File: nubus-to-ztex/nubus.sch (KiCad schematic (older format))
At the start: 54 parts, among them J4 0850030567 (DIN 41612C 3x32 p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, U1 74LVT125PW,118, U13 SN74CB3T3245PWR, U14 SN74CB3T3245PWR, U15 SN74CB3T3245PWR, U2 74LVT125PW,118, U3 74LVT125PW,118, U5 74LVT245BPW,118, U6 74LVT245BPW,118, U7 74LVT245BPW,118, U8 74LVT245BPW,118

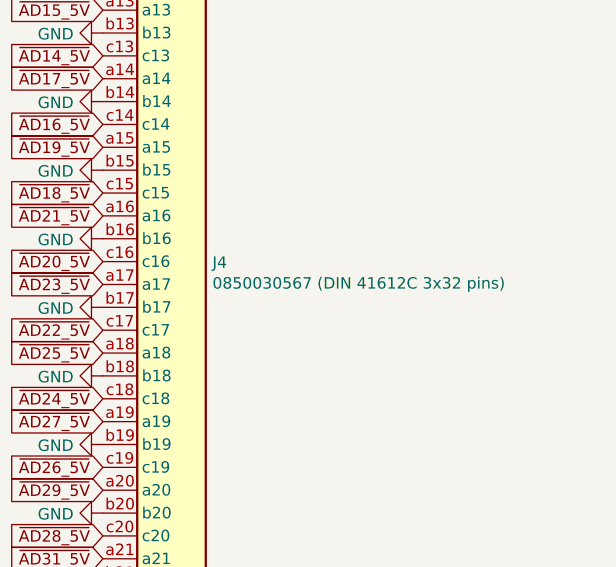
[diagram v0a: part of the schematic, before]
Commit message: more THT->SMT, lexx expensive parts/assembly (?)
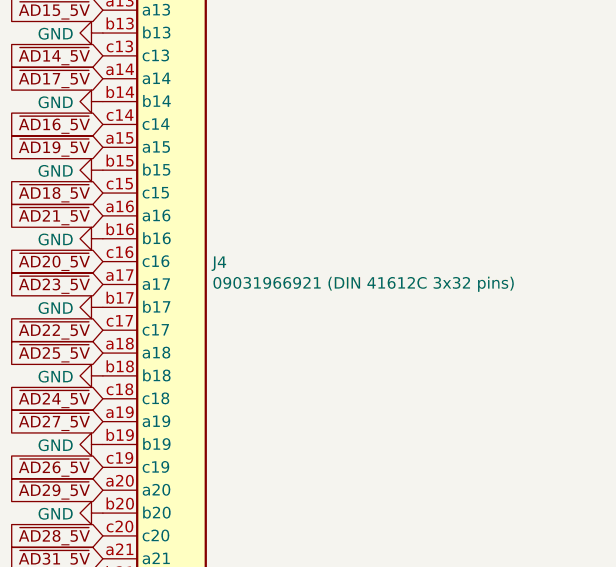
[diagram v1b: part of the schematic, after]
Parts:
- J4: value 0850030567 (DIN 41612C 3x32 pins) -> 09031966921 (DIN 41612C 3x32 pins); MPN 0850030567 -> 09033966921; MPN (Molex) (none) -> 85003-0567; MPN alias 85003-0567 -> (none); Notes (Harting) (none) -> Loads of variants...; URL https://www.mouser.fr/ProductDetail/Molex/85003-0567?qs=U4p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 -> https://www.mouser.fr/ProductDetail/HARTING/09031966921?qs=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
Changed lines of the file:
@@
 P 22250 5750
 F 0 "J4" H 22429 5846 50  0000 L CNN
-F 1 "0850030567 (DIN 41612C 3x32 pins)" H 22429 5755 50  0000 L CNN
+F 1 "09031966921 (DIN 41612C 3x32 pins)" H 22429 5755 50  0000 L CNN
 F 2 "For_SeeedStudio:DIN41612_C_3x32_Male_Horizontal_THT" H 22250 5800 50  0001 C CNN
 F 3 " ~" H 22250 5800 50  0001 C CNN
-F 4 "85003-0567" H 22250 5750 50  0001 C CNN "MPN alias"
-F 5 "https://www.mouser.fr/ProductDetail/Molex/85003-0567?qs=U4pz39agNJB6P1oBpJ4bJA%3D%3D" H 22250 5750 50  0001 C CNN "URL"
+F 4 "85003-0567" H 22250 5750 50  0001 C CNN "MPN (Molex)"
+F 5 "https://www.mouser.fr/ProductDetail/HARTING/09031966921?qs=gIpPgrDBK%2Fho4yEpoERymA%3D%3D" H 22250 5750 50  0001 C CNN "URL"
 F 6 "DIN-096CPC-RR1-HM" H 22250 5750 50  0001 C CNN "MPN (3M)"
 F 7 "RR1L would also work (for .062 PCBs)" H 22250 5750 50  0001 C CNN "Notes (3M)"
 F 8 "09033967921" H 22250 5750 50  0001 C CNN "MPN (Harting)"
 F 9 "09033966921" H 22250 5750 50  0001 C CNN "MPN (Harting 2)"
-F 10 "0850030567" H 22250 5750 50  0001 C CNN "MPN"
+F 10 "09033966921" H 22250 5750 50  0001 C CNN "MPN"
+F 11 "Loads of variants..." H 22250 5750 50  0001 C CNN "Notes (Harting)"
 	1    22250 5750
 	1    0    0    -1

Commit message: minor cleanups
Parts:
- C12, C14, C17, C18, C19, C30, C4, C5, C6, C8: LCSC ? -> (none)
- D10, D6, D7, D8, D9: value YELLOW Led -> YELLOW Led 0805
- D11, D12, D13, D14: value GREEN Led -> GREEN Led 0805
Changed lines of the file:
@@
 F 6 "603-CC603KRX7R8BB104" H 17550 2500 50  0001 C CNN "Mouser"
 F 7 "?" H 17550 2500 50  0001 C CNN "Digikey"
-F 8 "?" H 17550 2500 50  0001 C CNN "LCSC"
+F 8 "" H 17550 2500 50  0001 C CNN "LCSC"
 F 9 "?" H 17550 2500 50  0001 C CNN "Koncar"
 F 10 "TB" H 17550 2500 50  0001 C CNN "Side"
@@
 F 6 "603-CC603KRX7R8BB104" H 15550 2500 50  0001 C CNN "Mouser"
 F 7 "?" H 15550 2500 50  0001 C CNN "Digikey"
-F 8 "?" H 15550 2500 50  0001 C CNN "LCSC"
+F 8 "" H 15550 2500 50  0001 C CNN "LCSC"
 F 9 "?" H 15550 2500 50  0001 C CNN "Koncar"
 F 10 "TB" H 15550 2500 50  0001 C CNN "Side"
@@
 F 6 "603-CC603KRX7R8BB104" H 13500 2500 50  0001 C CNN "Mouser"
 F 7 "?" H 13500 2500 50  0001 C CNN "Digikey"
-F 8 "?" H 13500 2500 50  0001 C CNN "LCSC"
+F 8 "" H 13500 2500 50  0001 C CNN "LCSC"
 F 9 "?" H 13500 2500 50  0001 C CNN "Koncar"
 F 10 "TB" H 13500 2500 50  0001 C CNN "Side"
@@
 F 6 "603-CC603KRX7R8BB104" H 11450 2500 50  0001 C CNN "Mouser"
 F 7 "?" H 11450 2500 50  0001 C CNN "Digikey"
-F 8 "?" H 11450 2500 50  0001 C CNN "LCSC"
+F 8 "" H 11450 2500 50  0001 C CNN "LCSC"
 F 9 "?" H 11450 2500 50  0001 C CNN "Koncar"
 F 10 "TB" H 11450 2500 50  0001 C CNN "Side"
@@
 AR Path="/618F532C/61D85DFA" Ref="D11"  Part="1"
 F 0 "D11" H 16050 7950 50  0000 C CNN
-F 1 "GREEN Led" H 16100 7700 50  0000 R CNN
+F 1 "GREEN Led 0805" H 16100 7700 50  0000 R CNN
 F 2 "LED_SMD:LED_0805_2012Metric" H 16050 7850 50  0001 C CNN
 F 3 "https://www.lcsc.com/product-detail/Light-Emitting-Diodes-LED_Lite-On-LTST-C170KGKT_C98221.html" H 16050 7850 50  0001 C CNN
@@
 AR Path="/618F532C/61D85E17" Ref="D12"  Part="1"
 F 0 "D12" H 16050 8450 50  0000 C CNN
-F 1 "GREEN Led" H 16100 8200 50  0000 R CNN
+F 1 "GREEN Led 0805" H 16100 8200 50  0000 R CNN
 F 2 "LED_SMD:LED_0805_2012Metric" H 16050 8350 50  0001 C CNN
 F 3 "https://www.lcsc.com/product-detail/Light-Emitting-Diodes-LED_Lite-On-LTST-C170KGKT_C98221.html" H 16050 8350 50  0001 C CNN
@@
 AR Path="/618F532C/61D85E34" Ref="D13"  Part="1"
 F 0 "D13" H 16050 8950 50  0000 C CNN
-F 1 "GREEN Led" H 16100 8700 50  0000 R CNN
+F 1 "GREEN Led 0805" H 16100 8700 50  0000 R CNN
 F 2 "LED_SMD:LED_0805_2012Metric" H 16050 8850 50  0001 C CNN
 F 3 "https://www.lcsc.com/product-detail/Light-Emitting-Diodes-LED_Lite-On-LTST-C170KGKT_C98221.html" H 16050 8850 50  0001 C CNN
@@
 AR Path="/618F532C/61D85E51" Ref="D14"  Part="1"
 F 0 "D14" H 16050 9450 50  0000 C CNN
-F 1 "GREEN Led" H 16100 9200 50  0000 R CNN
+F 1 "GREEN Led 0805" H 16100 9200 50  0000 R CNN
 F 2 "LED_SMD:LED_0805_2012Metric" H 16050 9350 50  0001 C CNN
 F 3 "https://www.lcsc.com/product-detail/Light-Emitting-Diodes-LED_Lite-On-LTST-C170KGKT_C98221.html" H 16050 9350 50  0001 C CNN
@@
 F 6 "603-CC603KRX7R8BB104" H 5100 6200 50  0001 C CNN "Mouser"
 F 7 "?" H 5100 6200 50  0001 C CNN "Digikey"
-F 8 "?" H 5100 6200 50  0001 C CNN "LCSC"
+F 8 "" H 5100 6200 50  0001 C CNN "LCSC"
 F 9 "?" H 5100 6200 50  0001 C CNN "Koncar"
 F 10 "TB" H 5100 6200 50  0001 C CNN "Side"
@@
 F 6 "603-CC603KRX7R8BB104" H 4650 2850 50  0001 C CNN "Mouser"
 F 7 "?" H 4650 2850 50  0001 C CNN "Digikey"
-F 8 "?" H 4650 2850 50  0001 C CNN "LCSC"
+F 8 "" H 4650 2850 50  0001 C CNN "LCSC"
 F 9 "?" H 4650 2850 50  0001 C CNN "Koncar"
 F 10 "TB" H 4650 2850 50  0001 C CNN "Side"
@@
 F 6 "603-CC603KRX7R8BB104" H 4700 10300 50  0001 C CNN "Mouser"
 F 7 "?" H 4700 10300 50  0001 C CNN "Digikey"
-F 8 "?" H 4700 10300 50  0001 C CNN "LCSC"
+F 8 "" H 4700 10300 50  0001 C CNN "LCSC"
 F 9 "?" H 4700 10300 50  0001 C CNN "Koncar"
 F 10 "TB" H 4700 10300 50  0001 C CNN "Side"
@@
 F 6 "603-CC603KRX7R8BB104" H 5150 13300 50  0001 C CNN "Mouser"
 F 7 "?" H 5150 13300 50  0001 C CNN "Digikey"
-F 8 "?" H 5150 13300 50  0001 C CNN "LCSC"
+F 8 "" H 5150 13300 50  0001 C CNN "LCSC"
 F 9 "?" H 5150 13300 50  0001 C CNN "Koncar"
 F 10 "TB" H 5150 13300 50  0001 C CNN "Side"
@@
 AR Path="/6332A9A8/6332F9B3" Ref="D?"  Part="1"
 F 0 "D6" H 13000 7850 50  0000 C CNN
-F 1 "YELLOW Led" H 13050 7600 50  0000 R CNN
+F 1 "YELLOW Led 0805" H 13050 7600 50  0000 R CNN
 F 2 "LED_SMD:LED_0805_2012Metric" H 13000 7750 50  0001 C CNN
 F 3 "https://lcsc.com/product-detail/Light-Emitting-Diodes-LED_Lite-On-LTST-C170KSKT_C125091.html" H 13000 7750 50  0001 C CNN
@@
 AR Path="/6332A9A8/63342049" Ref="D?"  Part="1"
 F 0 "D9" H 13000 9100 50  0000 C CNN
-F 1 "YELLOW Led" H 13050 8850 50  0000 R CNN
+F 1 "YELLOW Led 0805" H 13050 8850 50  0000 R CNN
 F 2 "LED_SMD:LED_0805_2012Metric" H 13000 9000 50  0001 C CNN
 F 3 "https://lcsc.com/product-detail/Light-Emitting-Diodes-LED_Lite-On-LTST-C170KSKT_C125091.html" H 13000 9000 50  0001 C CNN
@@
 AR Path="/6332A9A8/63343356" Ref="D?"  Part="1"
 F 0 "D10" H 13000 9550 50  0000 C CNN
-F 1 "YELLOW Led" H 13050 9300 50  0000 R CNN
+F 1 "YELLOW Led 0805" H 13050 9300 50  0000 R CNN
 F 2 "LED_SMD:LED_0805_2012Metric" H 13000 9450 50  0001 C CNN
 F 3 "https://lcsc.com/product-detail/Light-Emitting-Diodes-LED_Lite-On-LTST-C170KSKT_C125091.html" H 13000 9450 50  0001 C CNN
@@
 AR Path="/6332A9A8/6334A05C" Ref="D?"  Part="1"
 F 0 "D7" H 13000 8250 50  0000 C CNN
-F 1 "YELLOW Led" H 13050 8000 50  0000 R CNN
+F 1 "YELLOW Led 0805" H 13050 8000 50  0000 R CNN
 F 2 "LED_SMD:LED_0805_2012Metric" H 13000 8150 50  0001 C CNN
 F 3 "https://lcsc.com/product-detail/Light-Emitting-Diodes-LED_Lite-On-LTST-C170KSKT_C125091.html" H 13000 8150 50  0001 C CNN
@@
 AR Path="/6332A9A8/63352DC7" Ref="D?"  Part="1"
 F 0 "D8" H 13000 8650 50  0000 C CNN
-F 1 "YELLOW Led" H 13050 8400 50  0000 R CNN
+F 1 "YELLOW Led 0805" H 13050 8400 50  0000 R CNN
 F 2 "LED_SMD:LED_0805_2012Metric" H 13000 8550 50  0001 C CNN
 F 3 "https://lcsc.com/product-detail/Light-Emitting-Diodes-LED_Lite-On-LTST-C170KSKT_C125091.html" H 13000 8550 50  0001 C CNN
@@
 F 6 "603-CC603KRX7R8BB104" H 16150 13350 50  0001 C CNN "Mouser"
 F 7 "?" H 16150 13350 50  0001 C CNN "Digikey"
-F 8 "?" H 16150 13350 50  0001 C CNN "LCSC"
+F 8 "" H 16150 13350 50  0001 C CNN "LCSC"
 F 9 "?" H 16150 13350 50  0001 C CNN "Koncar"
 F 10 "TB" H 16150 13350 50  0001 C CNN "Side"
@@
 F 6 "603-CC603KRX7R8BB104" H 12850 13350 50  0001 C CNN "Mouser"
 F 7 "?" H 12850 13350 50  0001 C CNN "Digikey"
-F 8 "?" H 12850 13350 50  0001 C CNN "LCSC"
+F 8 "" H 12850 13350 50  0001 C CNN "LCSC"
 F 9 "?" H 12850 13350 50  0001 C CNN "Koncar"
 F 10 "TB" H 12850 13350 50  0001 C CNN "Side"

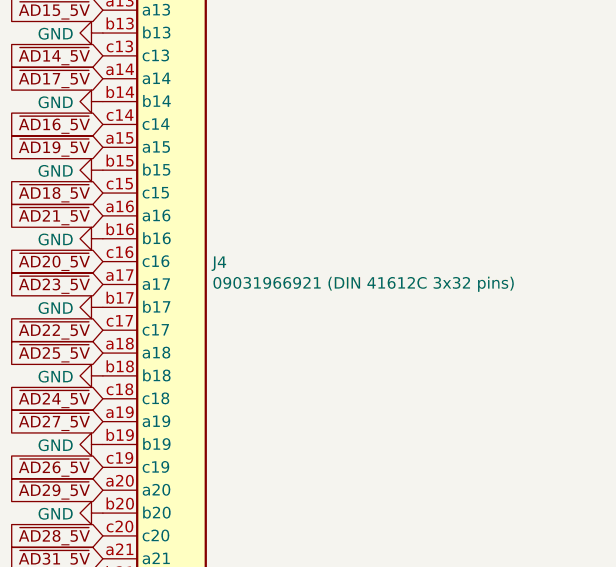
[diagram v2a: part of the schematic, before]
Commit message: BoM, power plane, serial back to THT, ...
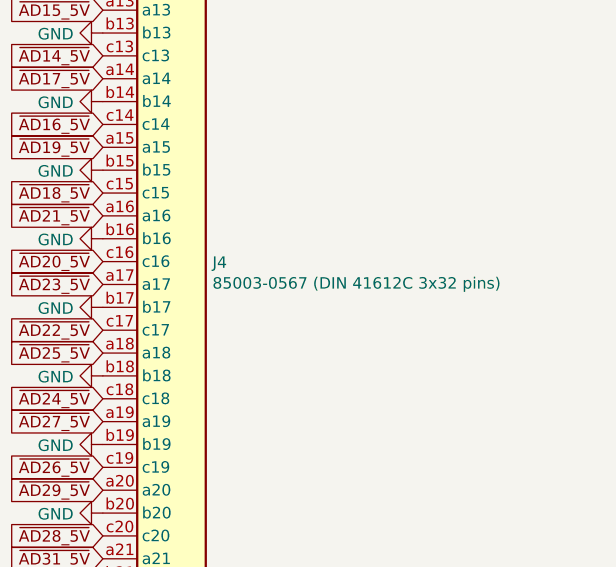
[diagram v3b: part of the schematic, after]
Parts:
- C12, C14, C17, C18, C19, C30, C4, C5, C6, C8: URL https://lcsc.com/product-detail/Multilayer-Ceramic-Capacito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 -> https://www.lcsc.com/product-detail/Multilayer-Ceramic-Capa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
- D10, D6, D7, D8, D9: URL https://lcsc.com/product-detail/Light-Emitting-Diodes-LED_L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 -> https://www.lcsc.com/product-detail/Light-Emitting-Diodes-L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
- J4: value 09031966921 (DIN 41612C 3x32 pins) -> 85003-0567 (DIN 41612C 3x32 pins); MPN 09033966921 -> 85003-0567; URL https://www.mouser.fr/ProductDetail/HARTING/09031966921?qs=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 -> https://www.lcsc.com/product-detail/Mezzanine-Connectors-Bo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; URL (Harting 2) (none) -> https://www.mouser.fr/ProductDetail/HARTING/09031966921?qs=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; URL (Molex) (none) -> https://www.lcsc.com/product-detail/Mezzanine-Connectors-Bo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
- R36, R37, R38, R39, R4, R40, R41, R42, R43, R44, R45, R5, R6, R7, R8: URL (none) -> https://www.lcsc.com/product-detail/Chip-Resistor-Surface-M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
- U1, U2, U3: URL https://eu.mouser.com/ProductDetail/Nexperia/74LVT125PW118?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 -> https://www.lcsc.com/product-detail/Buffer-Driver-Transceiv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
- U1, U2, U3: URL (none) -> https://www.lcsc.com/product-detail/Buffer-Driver-Transceiv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

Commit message: update
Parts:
- removed R8: 10k, Resistor_SMD:R_0603_1608Metric, symbol Device:R
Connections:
- net GND: now also D14.1 (K), U14.18 (B1), U14.2 (A1)
- net ~ID3_3V3: no longer D14.1 (K), U14.18 (B1)
- net ~ID3_5V: no longer U14.2 (A1)
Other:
- note added: "Also ID3 is always grounded (slots are $9-$E), so why waste a pin on it ?"
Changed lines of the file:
@@
 $Descr A2 23386 16535
 encoding utf-8
-Sheet 3 8
+Sheet 3 9
 Title "nubus-to-ztex NuBus connection & level shifting"
 Date ""
@@
 Text GLabel 2200 13850 0    50   Input ~ 0
 ~ID0_5V
-Text GLabel 2200 13550 0    50   Input ~ 0
-~ID3_5V
 Text GLabel 2200 13650 0    50   Input ~ 0
 ~ID2_5V
@@
 Text GLabel 3150 14350 0    50   Input ~ 0
 ~ID0_3V3
-Text GLabel 3150 14050 0    50   Input ~ 0
-~ID3_3V3
 Text GLabel 3150 14150 0    50   Input ~ 0
 ~ID2_3V3
@@
 $EndComp
 Wire Wire Line
-	15900 9350 15750 9350
-Wire Wire Line
 	16200 9350 16600 9350
 $Comp
@@
 Wire Wire Line
 	3150 13850 2250 13850
-$Comp
-L Device:R R?
-U 1 1 61AF68A2
-P 2550 14100
-AR Path="/5F6B165A/61AF68A2" Ref="R?"  Part="1"
-AR Path="/5F679B53/61AF68A2" Ref="R?"  Part="1"
-AR Path="/618F532C/61AF68A2" Ref="R8"  Part="1"
-F 0 "R8" V 2630 14100 50  0000 C CNN
-F 1 "10k" V 2550 14100 50  0000 C CNN
-F 2 "Resistor_SMD:R_0603_1608Metric" V 2480 14100 50  0001 C CNN
-F 3 "" H 2550 14100 50  0000 C CNN
-F 4 "0603WAF1002T5E" V 2550 13500 50  0001 C CNN "MPN"
-F 5 "https://www.lcsc.com/product-detail/Chip-Resistor-Surface-Mount_UNI-ROYAL-Uniroyal-Elec-0603WAF1002T5E_C25804.html" H 2550 14100 50  0001 C CNN "URL"
-	1    2550 14100
-	-1   0    0    -1
-$EndComp
-Wire Wire Line
-	2550 13550 2200 13550
 Wire Wire Line
 	2200 13650 2450 13650
@@
 Wire Wire Line
 	2450 13650 3150 13650
-Wire Wire Line
-	2450 14250 2550 14250
-Connection ~ 2450 14250
 Text GLabel 4350 6850 2    50   Input ~ 0
 ~ARB3_5V
@@
 Text Notes 2800 2750 2    50   ~ 0
 74LVT125 used for 'open collector'\n'Input' is tied low\n'/OE' is used as input\n'/OE' low -> enable -> output is low\n'/OE' high -> disable -> ouput is Z
-Wire Wire Line
-	2550 13950 2550 13550
-Connection ~ 2550 13550
 Text GLabel 3450 2750 0    50   Input ~ 0
 ~NMRQ_3V3
@@
 	1    0    0    -1
 $EndComp
-Wire Wire Line
-	2550 13550 3150 13550
 Text GLabel 4550 14350 2    50   Input ~ 0
 ~ARB1_3V3
@@
 $EndComp
 Connection ~ 7600 6150
+Text Notes 475  14525 0    50   ~ 0
+Also ID3 is always grounded (slots are $9-$E), so why waste a pin on it ?
+$Comp
+L power:GND #PWR0133
+U 1 1 64F61A19
+P 3150 13550
+F 0 "#PWR0133" H 3150 13300 50  0001 C CNN
+F 1 "GND" H 3155 13377 50  0000 C CNN
+F 2 "" H 3150 13550 50  0001 C CNN
+F 3 "" H 3150 13550 50  0001 C CNN
+	1    3150 13550
+	0    1    1    0
+$EndComp
+$Comp
+L power:GND #PWR0134
+U 1 1 64F61F6C
+P 3150 14050
+F 0 "#PWR0134" H 3150 13800 50  0001 C CNN
+F 1 "GND" H 3155 13877 50  0000 C CNN
+F 2 "" H 3150 14050 50  0001 C CNN
+F 3 "" H 3150 14050 50  0001 C CNN
+	1    3150 14050
+	0    1    1    0
+$EndComp
+$Comp
+L power:GND #PWR0135
+U 1 1 64F7A284
+P 15900 9350
+F 0 "#PWR0135" H 15900 9100 50  0001 C CNN
+F 1 "GND" H 15905 9177 50  0000 C CNN
+F 2 "" H 15900 9350 50  0001 C CNN
+F 3 "" H 15900 9350 50  0001 C CNN
+	1    15900 9350
+	1    0    0    -1
+$EndComp
 $EndSCHEMATC

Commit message: some BoM optimization
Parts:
- C12, C14, C17, C18, C19, C30, C4, C5, C6, C8: MPN CC0603KRX7R8BB104 -> CC0603KRX7R9BB104; URL https://www.lcsc.com/product-detail/Multilayer-Ceramic-Capacitors-MLCC-SMD-SMT_YAGEO-CC0603KRX7R8BB104_C92490.html -> https://www.lcsc.com/product-detail/Multilayer-Ceramic-Capacitors-MLCC-SMD-SMT_YAGEO-CC0603KRX7R9BB104_C14663.html
- D10, D6, D7, D8, D9: value YELLOW Led 0805 -> YELLOW Led 0603; footprint LED_SMD:LED_0805_2012Metric -> LED_SMD:LED_0603_1608Metric; MNF1_URL www.liteon.com -> (none); MPN LTST-C170KSKT -> 19-213/Y2C-CQ2R2L/3T(CY); URL https://www.lcsc.com/product-detail/Light-Emitting-Diodes-LED_Lite-On-LTST-C170KSKT_C125091.html -> https://www.lcsc.com/product-detail/Light-Emitting-Diodes-LED_Everlight-Elec-19-213-Y2C-CQ2R2L-3T-CY_C72038.html
- D11, D12, D13, D14: value GREEN Led 0805 -> GREEN Led 0603; footprint LED_SMD:LED_0805_2012Metric -> LED_SMD:LED_0603_1608Metric; MNF1_URL www.liteon.com -> (none); MPN LTST-C170KGKT -> 19-217/GHC-YR1S2/3T; URL https://www.lcsc.com/product-detail/Light-Emitting-Diodes-LED_Lite-On-LTST-C170KGKT_C98221.html -> https://www.lcsc.com/product-detail/Light-Emitting-Diodes-LED_Everlight-Elec-19-217-GHC-YR1S2-3T_C72043.html
- J4: MPN 85003-0567 -> 86093967113745ELF; MPN (Amphenol @ JLCPCB) (none) -> 86093967113745ELF
- R11, R12, R13, R14, R15, R16, R17, R18, R19: value 590 -> 560; MPN 0603WAF5900T5E -> 0603WAF5600T5E; URL https://www.lcsc.com/product-detail/Chip-Resistor-Surface-Mount_UNI-ROYAL-Uniroyal-Elec-0603WAF5900T5E_C23084.html -> https://www.lcsc.com/product-detail/Chip-Resistor-Surface-Mount_UNI-ROYAL-Uniroyal-Elec-0603WAF5600T5E_C23204.html
